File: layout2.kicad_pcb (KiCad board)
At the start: 2 copper layers, 23 parts, among them J1 RJ45, J2 RJ45, J3 RJ45, J4 RJ45, J5 RJ45, J6 RJ45, J7 RJ45, J8 RJ45, J9 Screw_Terminal_01x02, U1 74HC245, U2 74HC245, U3 Teensy4.1, U4 74HC245, U5 74HC245

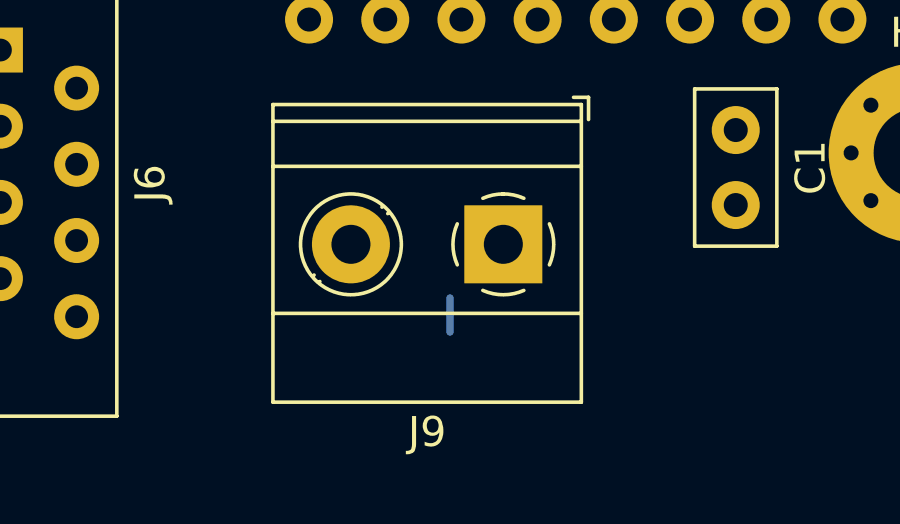
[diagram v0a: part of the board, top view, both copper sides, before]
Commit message: updated board layout, converted rj-45 ports to dual rj-45 ports Converted design to kicad 5.
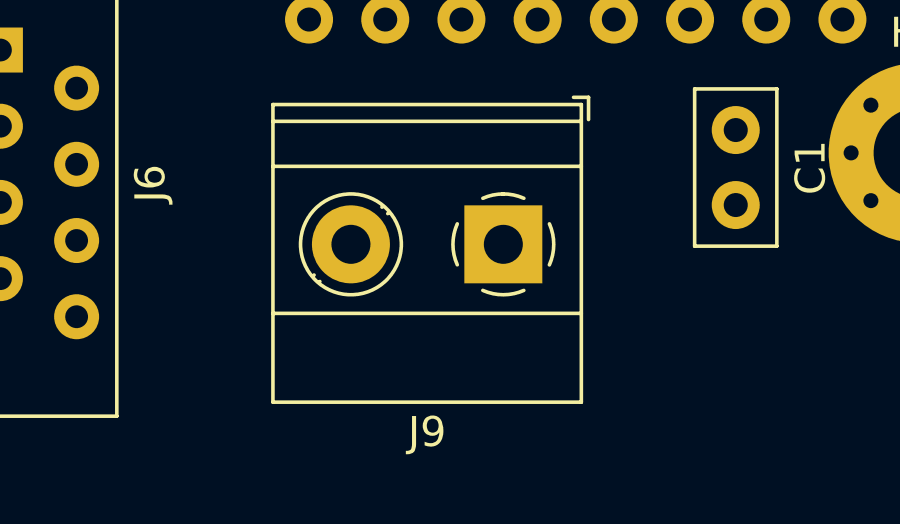
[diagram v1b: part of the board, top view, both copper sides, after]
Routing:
- net GND: track 1.13 -> 0.00 mm
